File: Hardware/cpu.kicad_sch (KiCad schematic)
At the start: 0 parts

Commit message: Rebuild p1_reader project
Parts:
- added C1: 100nF, Capacitor_SMD:C_0402_1005Metric, symbol Device:C_Small
- added C2, C3: 10uF, Capacitor_SMD:C_0402_1005Metric, symbol Device:C_Small
- added D1: 82400102, Package_TO_SOT_SMD:SOT-23-6, symbol manul_tech:82400102
- added J2: 629722000214, manul_tech:629722000214, symbol manul_tech:629722000214
- added R6, R7: 5.1K, Resistor_SMD:R_0402_1005Metric, symbol Device:R_Small
- added R8: 10K, Resistor_SMD:R_0402_1005Metric, symbol Device:R_Small
- added U3: ESP32-C3-WROOM-02U-N4, manul_tech:XCVR_ESP32-C3-WROOM-02U-N4, symbol manul_tech:ESP32-C3-WROOM-02U-N4
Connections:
- new net: J2.A5 (CC1), R6.2
- new net: J2.B5 (CC2), R7.1
- new net +3V3: C1.1, C2.1, R8.1, U3.1 (3V3)
- new net BOOT: U3.8 (IO9)
- new net D+: D1.1 (IO1), J2.A6 (D+1), J2.B6 (D+2)
- new net D-: D1.3 (IO2), J2.A7 (D-1), J2.B7 (D-2)
- new net DA+: D1.6 (IO1), U3.14 (IO19)
- new net DA-: D1.4 (IO2), U3.13 (IO18)
- new net DATA: U3.5 (IO6)
- new net EN: C3.1, R8.2, U3.2 (EN)
- new net GND: C1.2, C2.2, C3.2, D1.2 (GND), J2.A1 (GND), J2.A12 (GND), J2.S1 (SHIELD), J2.S2 (SHIELD), J2.S3 (SHIELD), J2.S4 (SHIELD), R6.1, R7.2, U3.19_1 (GND), U3.19_2 (GND), U3.19_3 (GND), U3.19_4 (GND), U3.19_5 (GND), U3.19_6 (GND), U3.19_7 (GND), U3.19_8 (GND), U3.19_9 (GND), U3.9 (GND)
- new net RQ: U3.4 (IO5)
- new net VBUS: D1.5 (VDD), J2.A4 (VBUS), J2.A9 (VBUS)
- no-connect marks 0 -> 10

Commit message: Schematic completed, started placing
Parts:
- removed U3: ESP32-C3-WROOM-02U-N4, manul_tech:XCVR_ESP32-C3-WROOM-02U-N4, symbol manul_tech:ESP32-C3-WROOM-02U-N4
- added U4: ESP32-C3-WROOM-02U-N4, manul_tech:MODULE_ESP32-C3-WROOM-02-H4, symbol manul_tech:ESP32-C3-WROOM-02-N4
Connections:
- net +3V3: now also U4.1 (3V3)
- net BOOT: now also U4.8 (IO9)
- net DA+: now also U4.14 (IO19)
- net DA-: now also U4.13 (IO18)
- net DATA: now also U4.5 (IO6)
- net EN: now also U4.2 (EN)
- net GND: now also U4.19_1 (GND), U4.19_2 (GND), U4.19_3 (GND), U4.19_4 (GND), U4.19_5 (GND), U4.19_6 (GND), U4.19_7 (GND), U4.19_8 (GND), U4.19_9 (GND), U4.9 (GND)
- net RQ: now also U4.4 (IO5)
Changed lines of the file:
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@@
-    )
-  )
-  (symbol (lib_id "manul_tech:ESP32-C3-WROOM-02U-N4") (at 124.46 66.04 0) (unit 1)
-    (in_bom yes) (on_board yes) (dnp no) (fields_autoplaced)
-    (property "Reference" "U3" (at 124.46 43.18 0)
-      (effects (font (size 1.27 1.27)))
-    )
-    (property "Value" "ESP32-C3-WROOM-02U-N4" (at 124.46 45.72 0)
-      (effects (font (size 1.27 1.27)))
-    )
-    (property "Footprint" "manul_tech:XCVR_ESP32-C3-WROOM-02U-N4" (at 124.46 66.04 0)
-      (effects (font (size 1.27 1.27)) (justify bottom) hide)
-    )
-    (property "Datasheet" "" (at 124.46 66.04 0)
-      (effects (font (size 1.27 1.27)) hide)
-    )
-    (pin "1")
-    (pin "10")
-    (pin "11")
-    (pin "12")
-    (pin "13")
-    (pin "14")
-    (pin "15")
-    (pin "16")
-    (pin "17")
-    (pin "18")
-    (pin "19_1")
-    (pin "19_2")
-    (pin "19_3")
-    (pin "19_4")
-    (pin "19_5")
-    (pin "19_6")
-    (pin "19_7")
-    (pin "19_8")
-    (pin "19_9")
-    (pin "2")
-    (pin "3")
-    (pin "4")
-    (pin "5")
-    (pin "6")
-    (pin "7")
-    (pin "8")
-    (pin "9")
-    (instances
-      (project "sp1_communicator"
-        (path "/d9bd008b-84e8-4d0b-9177-df1b9a254894/09d88c85-f555-474c-9d74-2222a962560f"
-          (reference "U3") (unit 1)
-        )
-      )
     )
   )
@@
         )
       )
+    )
+  )
+  (symbol (lib_id "manul_tech:ESP32-C3-WROOM-02-N4") (at 124.46 66.04 0) (unit 1)
+    (in_bom yes) (on_board yes) (dnp no) (fields_autoplaced)
+    (property "Reference" "U4" (at 124.46 43.18 0)
+      (effects (font (size 1.27 1.27)))
+    )
+    (property "Value" "ESP32-C3-WROOM-02U-N4" (at 124.46 45.72 0)
+      (effects (font (size 1.27 1.27)))
+    )
+    (property "Footprint" "manul_tech:MODULE_ESP32-C3-WROOM-02-H4" (at 124.46 66.04 0)
+      (effects (font (size 1.27 1.27)) (justify bottom) hide)
+    )
+    (property "Datasheet" "" (at 124.46 66.04 0)
+      (effects (font (size 1.27 1.27)) hide)
+    )
+    (pin "19_7")
+    (pin "10")
+    (pin "6")
+    (pin "19_8")
+    (pin "12")
+    (pin "18")
+    (pin "19_1")
+    (pin "19_9")
+    (pin "2")
+    (pin "9")
+    (pin "13")
+    (pin "1")
+    (pin "17")
+    (pin "3")
+    (pin "14")
+    (pin "15")
+    (pin "4")
+    (pin "19_6")
+    (pin "19_2")
+    (pin "8")
+    (pin "7")
+    (pin "19_4")
+    (pin "19_3")
+    (pin "5")
+    (pin "16")
+    (pin "19_5")
+    (pin "11")
+    (instances
+      (project "sp1_communicator"
+        (path "/d9bd008b-84e8-4d0b-9177-df1b9a254894/09d88c85-f555-474c-9d74-2222a962560f"
+          (reference "U4") (unit 1)
+        )
+      )

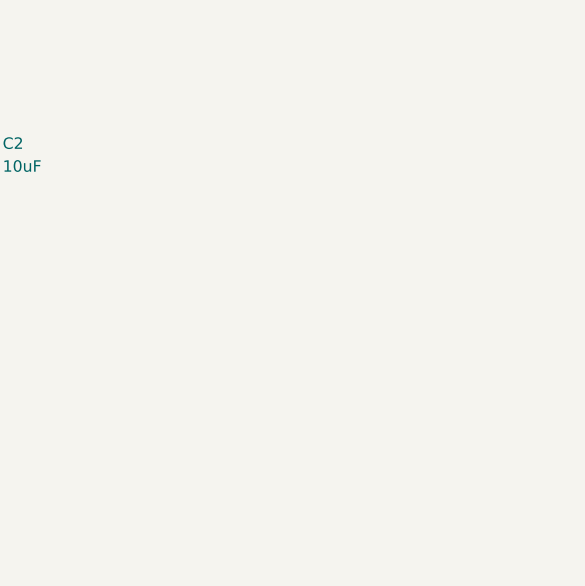
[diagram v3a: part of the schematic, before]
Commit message: Completed routing
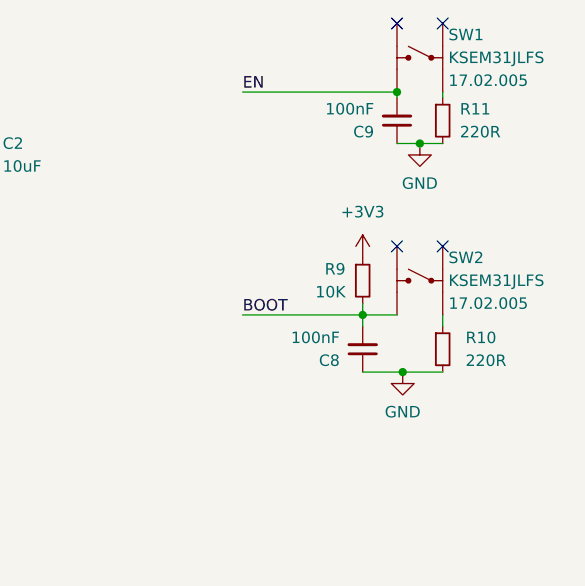
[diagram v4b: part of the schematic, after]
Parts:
- added C8, C9: 100nF, Capacitor_SMD:C_0402_1005Metric, symbol Device:C_Small
- added R10, R11: 220R, Resistor_SMD:R_0402_1005Metric, symbol Device:R_Small
- added R9: 10K, Resistor_SMD:R_0402_1005Metric, symbol Device:R_Small
- added SW1, SW2: KSEM31JLFS, manul_tech:KSEM31JLFS, symbol manul_tech:KSEM31JLFS
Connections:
- net +3V3: now also R9.1
- net BOOT: now also C8.2, R9.2, SW2.1
- net EN: now also C9.2, SW1.1
- net GND: now also C8.1, C9.1, R10.2, R11.2
- new net: R11.1, SW1.3
- new net: R10.1, SW2.3
- no-connect marks 10 -> 14

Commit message: completed routing
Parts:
- removed C1, C8, C9: 100nF, Capacitor_SMD:C_0402_1005Metric, symbol Device:C_Small
- removed C2, C3: 10uF, Capacitor_SMD:C_0402_1005Metric, symbol Device:C_Small
- removed D1: 82400102, Package_TO_SOT_SMD:SOT-23-6, symbol manul_tech:82400102
- removed J2: 629722000214, manul_tech:629722000214, symbol manul_tech:629722000214
- removed R10, R11: 220R, Resistor_SMD:R_0402_1005Metric, symbol Device:R_Small
- removed R6, R7: 5.1K, Resistor_SMD:R_0402_1005Metric, symbol Device:R_Small
- removed R8, R9: 10K, Resistor_SMD:R_0402_1005Metric, symbol Device:R_Small
- removed SW1, SW2: KSEM31JLFS, manul_tech:KSEM31JLFS, symbol manul_tech:KSEM31JLFS
- removed U4: ESP32-C3-WROOM-02U-N4, manul_tech:MODULE_ESP32-C3-WROOM-02-H4, symbol manul_tech:ESP32-C3-WROOM-02-N4
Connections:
- no-connect marks 14 -> 0
